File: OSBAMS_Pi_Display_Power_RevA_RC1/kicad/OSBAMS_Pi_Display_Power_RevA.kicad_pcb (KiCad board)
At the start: 2 copper layers, 100 x 70 mm, 25 parts, among them U1 RSDW40F-05

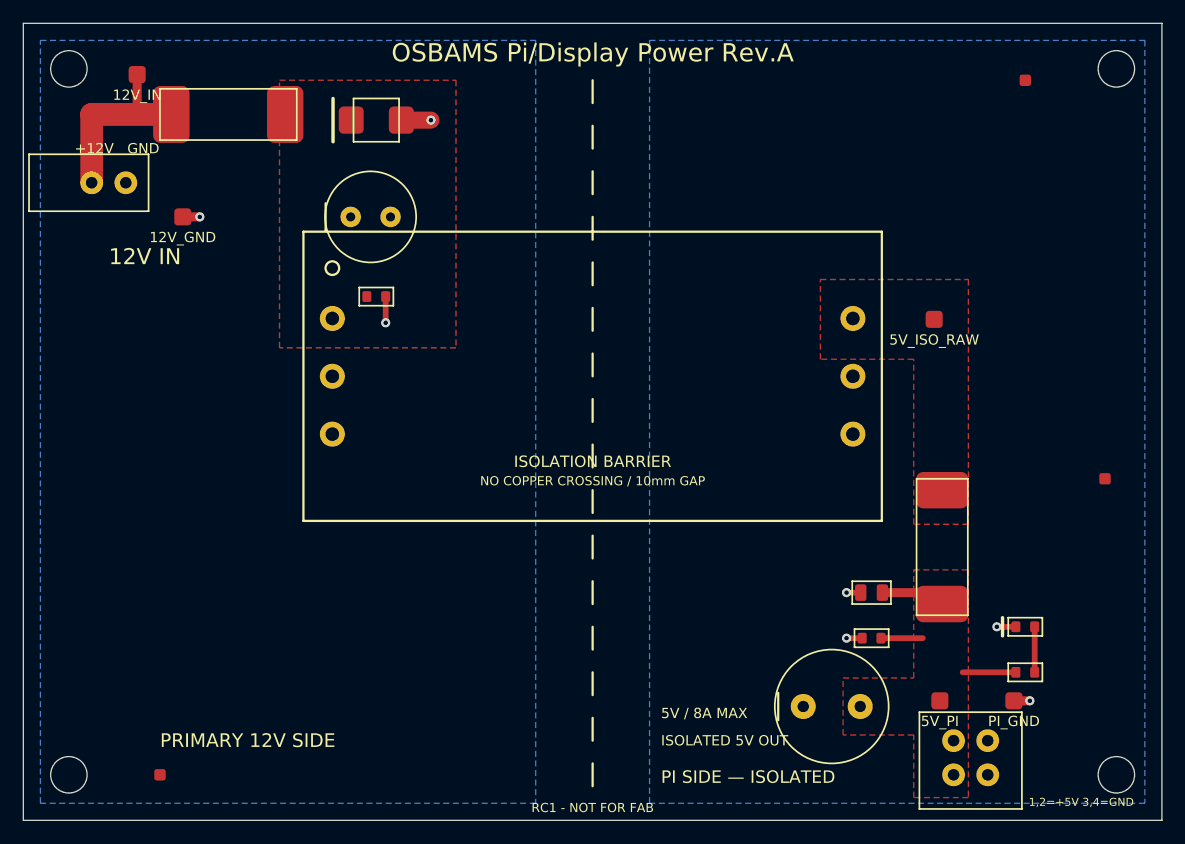
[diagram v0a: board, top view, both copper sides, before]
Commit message: Pi/Display power board RC1.1: library footprints, 5V drop budget, DNP trim pads
Replace hand-drawn footprints with official KiCad ones (fixes Micro-Fit
row numbering and Nano2 size), re-lay the 5V path, add voltage-drop budget
script/doc, 16 AWG/150 mm harness, DNP trim network. RSDW40F-05 footprint is
still an unverified placeholder; RC2 intentionally not generated.

Co-Authored-By: Claude Sonnet 5.5 <noreply@anthropic.com>
Claude-Session: https://claude.ai/code/session_01ENatZXrEDA18PaxUrZWrpi
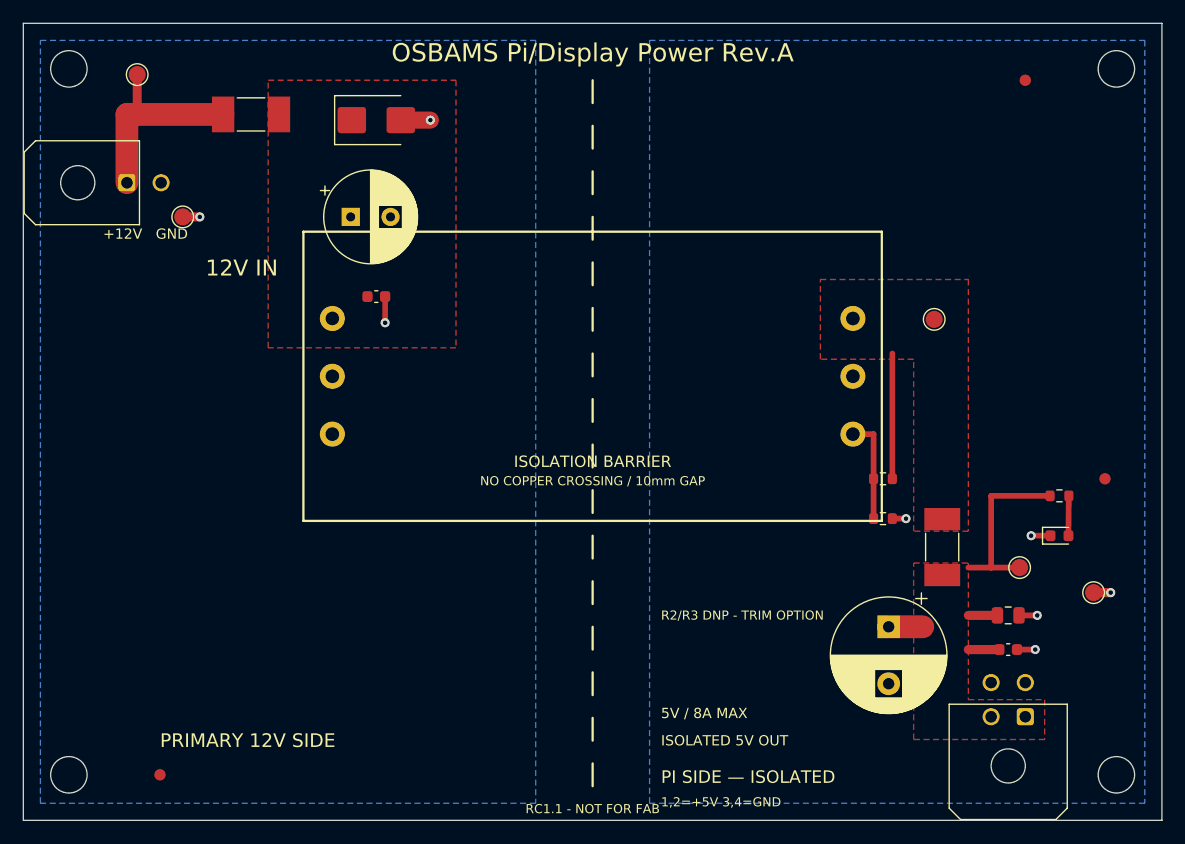
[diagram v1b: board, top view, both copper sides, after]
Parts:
- removed the J_IN at (6.00, 14.0)
- removed the J_OUT at (81.7, 63.0)
- added J_IN: 12V IN, Connector_Molex:Molex_Micro-Fit_3.0_43045-0200_2x01_P3.00mm_Horizontal, F.Cu at (9.10, 14.0)
- added J_OUT: ISOLATED 5V OUT, Connector_Molex:Molex_Micro-Fit_3.0_43045-0400_2x02_P3.00mm_Horizontal, F.Cu at (88.0, 60.9)
- added R2: DNP, Resistor_SMD:R_0603_1608Metric, F.Cu at (75.5, 40.0)
- added R3: DNP, Resistor_SMD:R_0603_1608Metric, F.Cu at (75.5, 43.5)
- C1, C6: footprint OSBAMS_PiPwr:C0603 -> Capacitor_SMD:C_0603_1608Metric
- C2: footprint OSBAMS_PiPwr:CP_RADIAL_D8_P35 -> Capacitor_THT:CP_Radial_D8.0mm_P3.50mm
- C4: footprint OSBAMS_PiPwr:CP_RADIAL_D10_P50 -> Capacitor_THT:CP_Radial_D10.0mm_P5.00mm
- C5: footprint OSBAMS_PiPwr:C0805 -> Capacitor_SMD:C_0805_2012Metric
- D1: footprint OSBAMS_PiPwr:LED0603 -> LED_SMD:LED_0603_1608Metric
- F1: footprint OSBAMS_PiPwr:FUSE_NANO2_H -> Fuse:Fuse_Littelfuse-NANO2-451_453
- F2: footprint OSBAMS_PiPwr:FUSE_NANO2_V -> Fuse:Fuse_Littelfuse-NANO2-451_453
- FID1, FID2, FID3: value FID -> Fiducial_1mm_Mask2mm; footprint OSBAMS_PiPwr:FIDUCIAL_1MM -> Fiducial:Fiducial_1mm_Mask2mm
- H1, H2, H3, H4: value M3 -> MountingHole_3.2mm_M3; footprint OSBAMS_PiPwr:MountingHole_3.2mm_M3 -> MountingHole:MountingHole_3.2mm_M3
- R1: footprint OSBAMS_PiPwr:R0603 -> Resistor_SMD:R_0603_1608Metric
- TP1, TP2, TP3, TP4, TP5: footprint OSBAMS_PiPwr:TP15 -> TestPoint:TestPoint_Pad_D1.5mm
- TVS1: footprint OSBAMS_PiPwr:DO214AA -> Diode_SMD:D_SMB
- U1: footprint OSBAMS_PiPwr:RSDW40_PLACEHOLDER -> OSBAMS_PiPwr:RSDW40F-05_PLACEHOLDER_UNVERIFIED
- moved R1 15.8 mm to (91.0, 41.5)
- moved TP4 13.6 mm to (87.5, 47.8)
- moved C5 12.2 mm to (86.5, 52.0)
- moved C6 12.0 mm to (86.5, 55.0)
- moved TP5 11.8 mm to (94.0, 50.0)
- moved C4 8.60 mm to (76.0, 53.0), turned to -90 degrees
- moved D1 8.54 mm to (91.0, 45.0)
- moved F1 2.00 mm to (20.0, 8.00)
- moved C2 1.75 mm to (28.8, 17.0)
- turned F2 to -90 degrees
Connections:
- C5 pad 1: PI_GND -> 5V_PI
- C5 pad 2: 5V_PI -> PI_GND
- C6 pad 1: PI_GND -> 5V_PI
- C6 pad 2: 5V_PI -> PI_GND
- U1 pad 6: (no net) -> TRIM
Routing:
- net 5V_PI: track 11.9 -> 24.2 mm
- net 5V_ISO_RAW: track 0.00 -> 11.0 mm
- net TRIM: track 0.00 -> 9.23 mm
- net PI_GND: track 5.70 -> 7.60 mm, vias 4 -> 5
- net +12V_IN: track 16.5 -> 17.9 mm
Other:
- board text added: "R2/R3 DNP - TRIM OPTION"
- board text added: "RC1.1 - NOT FOR FAB"
- board text removed: "RC1 - NOT FOR FAB"

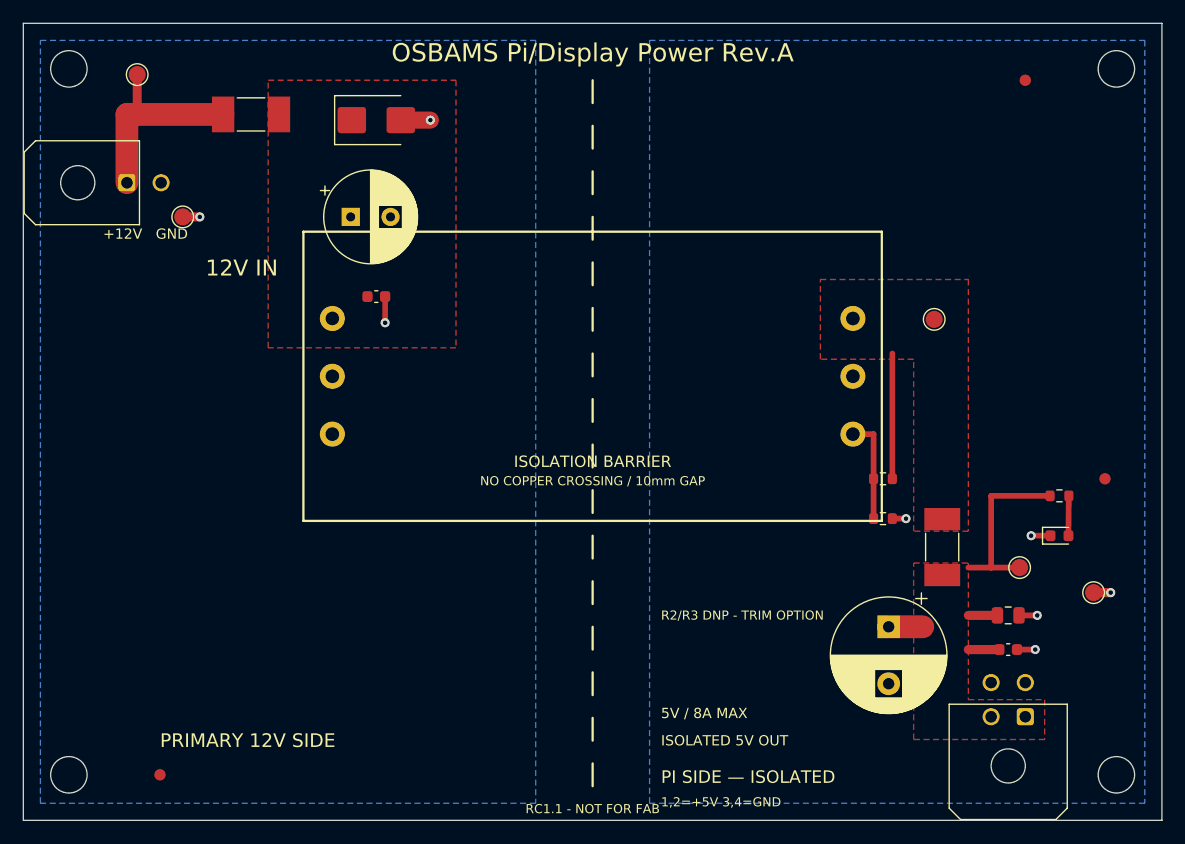
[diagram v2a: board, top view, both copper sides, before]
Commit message: U1 footprint from Mean Well drawing; datasheet tolerance stack; findings
Layout redone around the real RSDW40 pin pattern. Budget now uses accuracy+line+load+tempco: closes by ~2 mV at 25 C, fails with temperature rise unless calibrated. Flags F1 vs recommended 8 A delay fuse; Harwin contact verified (no resistance figure in file).

Co-Authored-By: Claude Sonnet 5.5 <noreply@anthropic.com>
Claude-Session: https://claude.ai/code/session_01ENatZXrEDA18PaxUrZWrpi
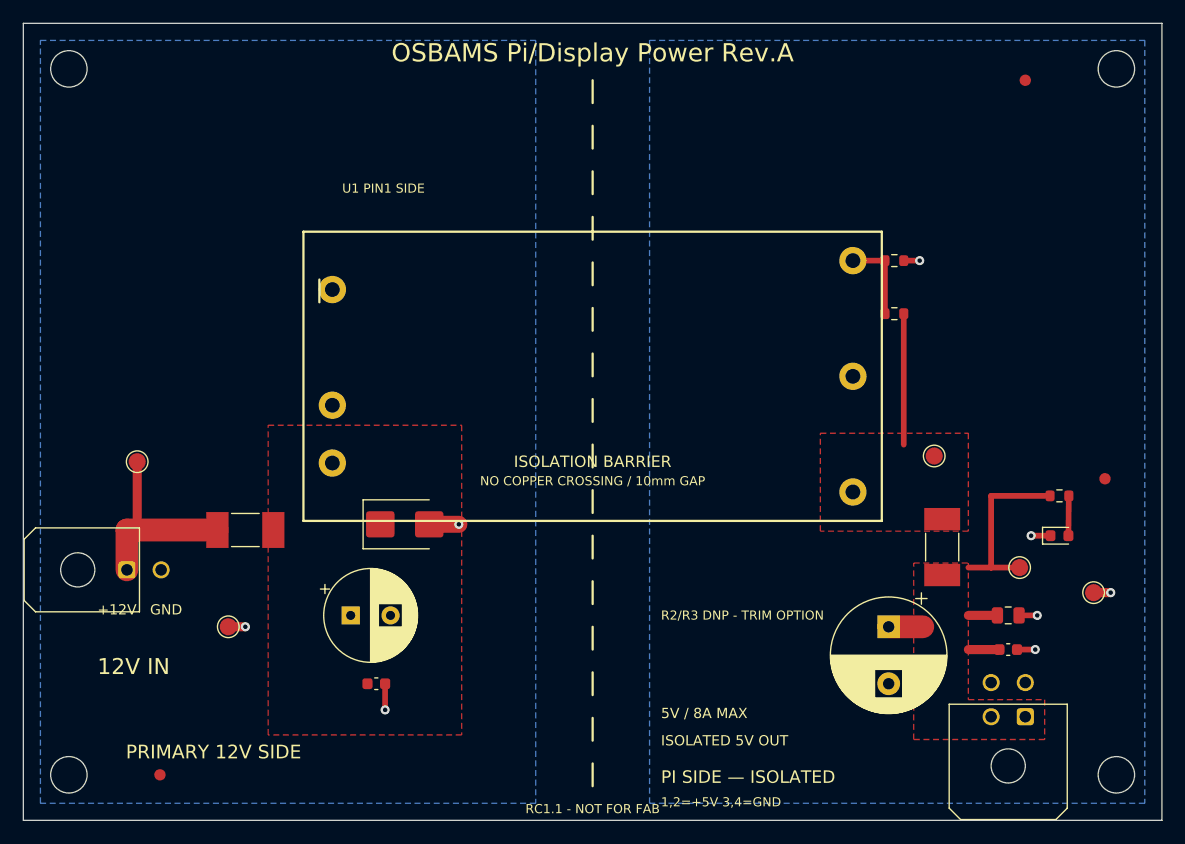
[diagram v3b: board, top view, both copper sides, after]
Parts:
- U1: footprint OSBAMS_PiPwr:RSDW40F-05_PLACEHOLDER_UNVERIFIED -> OSBAMS_PiPwr:RSDW40F-05_MeanWell_2x1in
- moved F1 36.5 mm to (19.5, 44.5)
- moved TP2 36.2 mm to (18.0, 53.0)
- moved TVS1 35.6 mm to (33.5, 44.0)
- moved C2 35.0 mm to (28.8, 52.0)
- moved C1 34.0 mm to (31.0, 58.0)
- moved J_IN 34.0 mm to (9.10, 48.0)
- moved TP1 34.0 mm to (10.0, 38.5)
- moved R3 22.7 mm to (76.5, 20.8)
- moved R2 14.5 mm to (76.5, 25.5)
- moved TP3 12.0 mm to (80.0, 38.0)
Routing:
- net TRIM: track 9.23 -> 7.47 mm
- net 5V_ISO_RAW: track 11.0 -> 11.5 mm
- net +12V_IN: track 17.9 -> 17.4 mm
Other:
- board text added: "U1 PIN1 SIDE"

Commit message: Keyed Pi interposer, F1 8A time-delay, calibration procedure, budget update
Add OSBAMS_Pi_Power_Interposer_RevA_RC1 (Micro-Fit + 2x20 stacking socket, key
standoffs), trim calibration script/procedure/acceptance record, F1 candidate
0453008.MRL, budget with interposer path. RC2 still gated: F1 datasheet,
socket MPN, key 3D check, KiCad 10 ERC.

Co-Authored-By: Claude Sonnet 5.5 <noreply@anthropic.com>
Claude-Session: https://claude.ai/code/session_01ENatZXrEDA18PaxUrZWrpi
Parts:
- F1: value 5A 125V -> 8A 125V TD

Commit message: F1 -> Littelfuse 407 8A time-lag (0407008.WR); F2 verified; interposer to HAT+ geometry
Remove 0453008.MRL (very fast-acting). F1 datasheet values and 1206 land pattern
implemented; F2 footprint verified against 451/453 datasheet. Interposer now 65 mm
with M2.5 mounting holes per HAT+ spec. RC2 still gated: socket MPN, Pi 5 STEP
keying check, KiCad 10 ERC.

Co-Authored-By: Claude Sonnet 5.5 <noreply@anthropic.com>
Claude-Session: https://claude.ai/code/session_01ENatZXrEDA18PaxUrZWrpi
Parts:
- F1: value 8A 125V TD -> 0407008.WR; footprint Fuse:Fuse_Littelfuse-NANO2-451_453 -> OSBAMS_PiPwr:Fuse_1206_Littelfuse407
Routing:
- net +12V_IN: track 17.4 -> 18.6 mm
